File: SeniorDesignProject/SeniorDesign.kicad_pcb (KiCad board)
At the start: 2 copper layers, 33 parts, among them J1 RJ45(LoadCells), J2 RJ45(Accelerometer), J3 PICkit3, J5 ID-12LA Header, J6 XBEE Header, J7 7-Segment Display, P7 Power 1, P9 Power 2, U1 INA827, U2 LM1117-3.3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

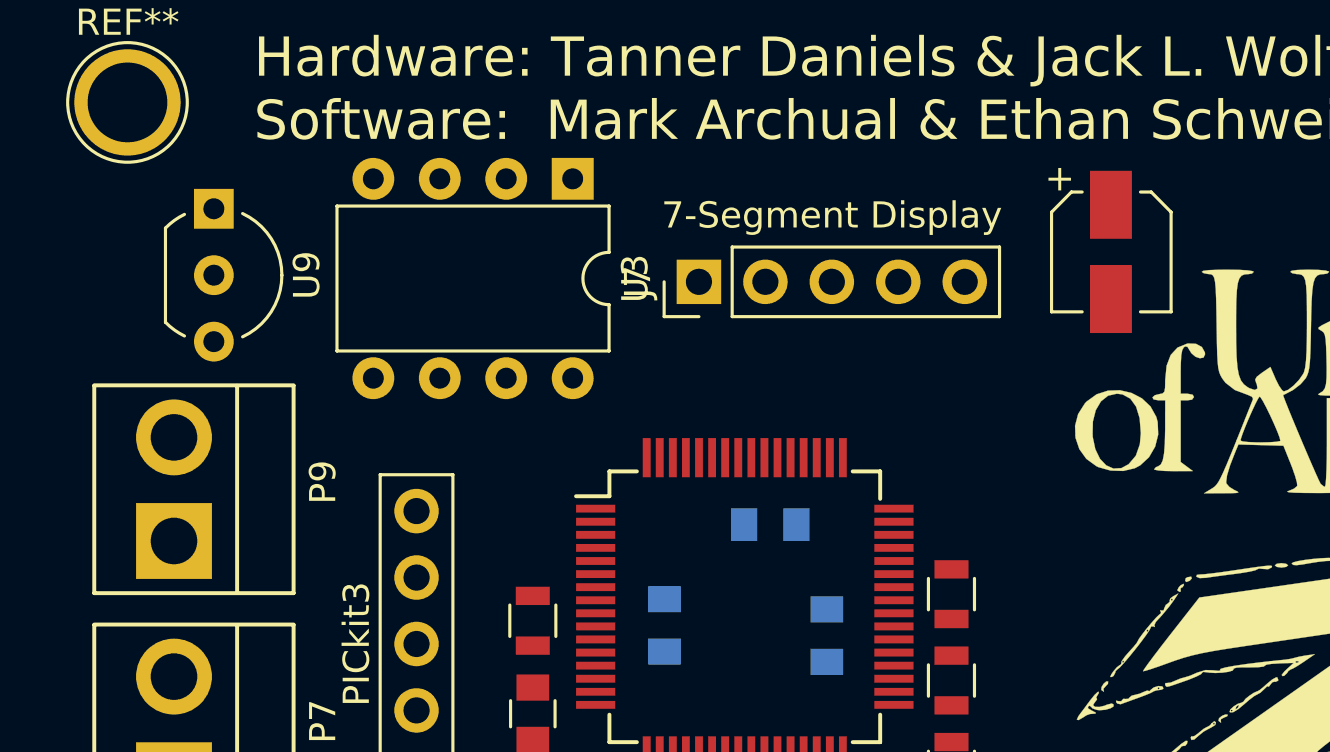
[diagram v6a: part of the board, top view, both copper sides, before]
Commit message: Added TC7660 +5V to -5V converter Removed -9V power Removed 7905 -9V to -5V regulator
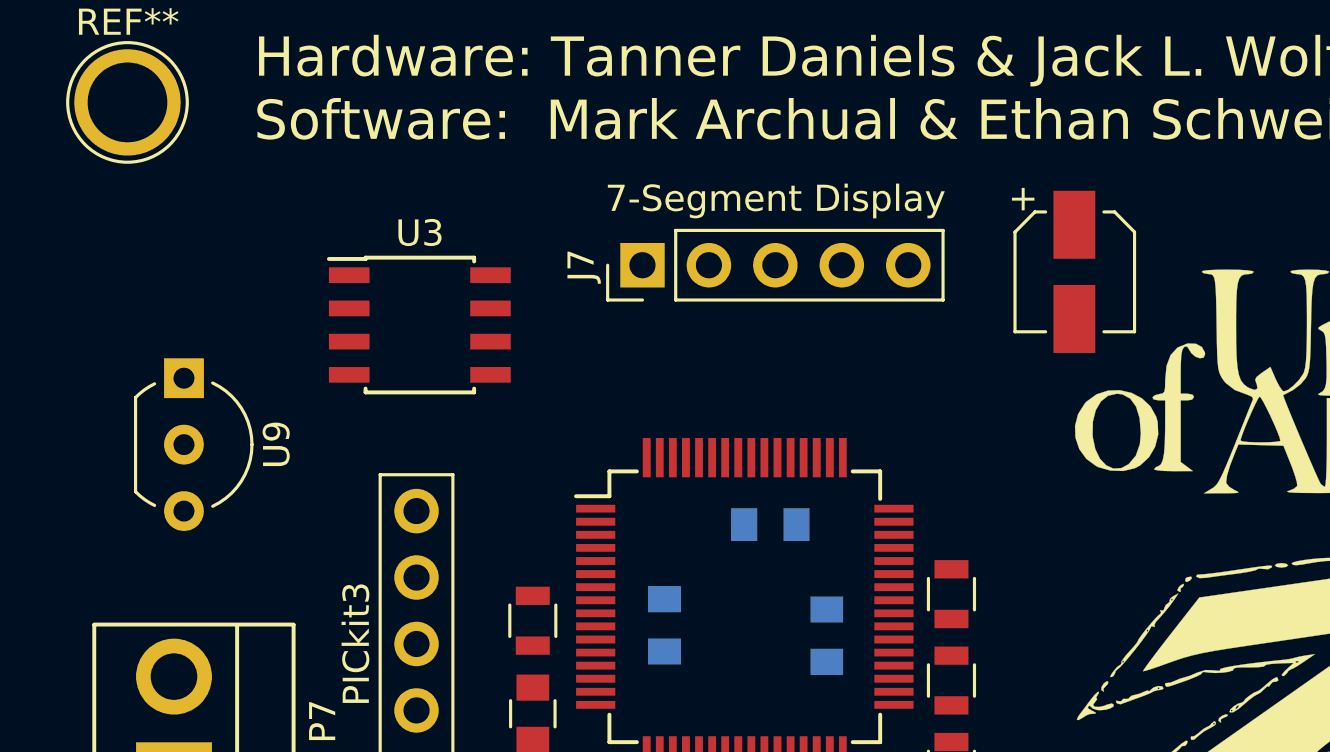
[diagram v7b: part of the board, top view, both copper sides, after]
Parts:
- removed P9: Power 2, Pin_Headers:Pin_Header_Straight_1x02_Pitch3.96mm_Friction_Lock
- U3: footprint Housings_DIP:DIP-8_W7.62mm -> Housings_SOIC:SOIC-8_3.9x4.9mm_Pitch1.27mm
- moved U3 8.08 mm to (131.3, 68.7), turned to 0 degrees
- moved U9 6.58 mm to (122.3, 70.7)
- moved J7 2.25 mm to (139.8, 66.4)
- moved C8 1.59 mm to (156.3, 66.7)
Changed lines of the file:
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@@
 (kicad_pcb (version 4) (host pcbnew 4.0.6-e0-6349~53~ubuntu16.04.1)
   (general
-    (links 66)
-    (no_connects 66)
-    (area 116.739999 56.175 186.028001 121.766001)
+    (links 65)
+    (no_connects 65)
+    (area 0 0 0 0)
     (thickness 1.6)
     (drawings 6)
     (tracks 2)
     (zones 0)
-    (modules 33)
-    (nets 103)
+    (modules 32)
+    (nets 102)
   )
   (page USLetter)
@@
   (net 95 "Net-(CPU1-Pad51)")
   (net 96 +9V)
-  (net 97 -9V)
-  (net 98 "Net-(U3-Pad1)")
-  (net 99 "Net-(U3-Pad2)")
-  (net 100 "Net-(U3-Pad6)")
-  (net 101 "Net-(U3-Pad7)")
-  (net 102 "Net-(U3-Pad4)")
+  (net 97 "Net-(U3-Pad1)")
+  (net 98 "Net-(U3-Pad2)")
+  (net 99 "Net-(U3-Pad6)")
+  (net 100 "Net-(U3-Pad7)")
+  (net 101 "Net-(U3-Pad4)")
   (net_class Default "This is the default net class."
     (clearance 0.2)
@@
     (add_net +9V)
     (add_net -5V)
-    (add_net -9V)
     (add_net 3.3V)
     (add_net A+)
@@
   )
   (module Capacitors_SMD:CP_Elec_4x4.5 (layer F.Cu)
-    (at 157.734 65.913 270)
+    (at 156.337 66.675 270)
     (descr "SMT capacitor, aluminium electrolytic, 4x4.5")
     (attr smd)
@@
     (pad 2 thru_hole circle (at 3.96 0 90) (size 2.9 2.9) (drill 1.78) (layers *.Cu *.Mask)
       (net 96 +9V))
-    (model Pin_Headers.3dshapes/Pin_Header_Straight_1x02_Pitch3.96mm_Friction_Lock.wrl
-      (at (xyz 0.08 0 0.125))
-      (scale (xyz 0.39 0.39 0.39))
-      (rotate (xyz 0 0 180))
-    )
-  )
-  (module Pin_Headers:Pin_Header_Straight_1x02_Pitch3.96mm_Friction_Lock (layer F.Cu)
-    (at 121.92 76.962 90)
-    (descr "Header Pin, Unshrouded, Friction Lock, Pitch 0.156\" (3.96mm)")
-    (tags "Pin Header Straight 1x02 Pitch3.96mm 640445-2")
-    (fp_text reference P9 (at 2.25 5.7 90) (layer F.SilkS)
-      (effects (font (size 1 1) (thickness 0.15)))
-    )
-    (fp_text value "Power 2" (at 2.45 -4.15 90) (layer F.Fab)
-      (effects (font (size 1 1) (thickness 0.15)))
-    )
-    (fp_line (start -2.25 -3.3) (end 6.2 -3.3) (layer F.CrtYd) (width 0.05))
-    (fp_line (start 6.2 -3.3) (end 6.2 4.85) (layer F.CrtYd) (width 0.05))
-    (fp_line (start 6.2 4.85) (end -2.25 4.85) (layer F.CrtYd) (width 0.05))
-    (fp_line (start -2.25 4.85) (end -2.25 -3.3) (layer F.CrtYd) (width 0.05))
-    (fp_line (start -1.9939 -3.048) (end 5.9309 -3.048) (layer F.SilkS) (width 0.15))
-    (fp_line (start -1.9939 4.572) (end 5.9309 4.572) (layer F.SilkS) (width 0.15))
-    (fp_line (start -1.9939 2.413) (end 5.9309 2.413) (layer F.SilkS) (width 0.15))
-    (fp_line (start 5.95 -3.048) (end 5.95 4.572) (layer F.SilkS) (width 0.15))
-    (fp_line (start -1.9939 -3.048) (end -1.9939 4.572) (layer F.SilkS) (width 0.15))
-    (pad 1 thru_hole rect (at 0 0 90) (size 2.9 2.9) (drill 1.78) (layers *.Cu *.Mask)
-      (net 97 -9V))
-    (pad 2 thru_hole circle (at 3.96 0 90) (size 2.9 2.9) (drill 1.78) (layers *.Cu *.Mask)
-      (net 45 GND))
     (model Pin_Headers.3dshapes/Pin_Header_Straight_1x02_Pitch3.96mm_Friction_Lock.wrl
       (at (xyz 0.08 0 0.125))
@@
   )
   (module Socket_Strips:Socket_Strip_Straight_1x05_Pitch2.54mm (layer F.Cu)
-    (at 141.986 67.056 90)
+    (at 139.827 66.421 90)
     (descr "Through hole straight socket strip, 1x05, 2.54mm pitch, single row")
     (tags "Through hole socket strip THT 1x05 2.54mm single row")
@@
   )
   (module TO_SOT_Packages_THT:TO-92_Inline_Wide (layer F.Cu)
-    (at 123.444 64.262 270)
+    (at 122.301 70.739 270)
     (descr "TO-92 leads in-line, wide, drill 0.8mm (see NXP sot054_po.pdf)")
     (tags "to-92 sc-43 sc-43a sot54 PA33 transistor")
@@
     (pad 1 thru_hole circle (at 0 0) (size 4.064 4.064) (drill 3.048) (layers *.Cu *.Mask))
   )
-  (module Housings_DIP:DIP-8_W7.62mm (layer F.Cu)
-    (at 137.16 63.119 270)
-    (descr "8-lead dip package, row spacing 7.62 mm (300 mils)")
-    (tags "DIL DIP PDIP 2.54mm 7.62mm 300mil")
-    (fp_text reference U3 (at 3.81 -2.39 270) (layer F.SilkS)
-      (effects (font (size 1 1) (thickness 0.15)))
-    )
-    (fp_text value ICL7660 (at 3.81 10.01 270) (layer F.Fab)
-      (effects (font (size 1 1) (thickness 0.15)))
-    )
-    (fp_arc (start 3.81 -1.39) (end 2.81 -1.39) (angle -180) (layer F.SilkS) (width 0.12))
-    (fp_line (start 1.635 -1.27) (end 6.985 -1.27) (layer F.Fab) (width 0.1))
-    (fp_line (start 6.985 -1.27) (end 6.985 8.89) (layer F.Fab) (width 0.1))
-    (fp_line (start 6.985 8.89) (end 0.635 8.89) (layer F.Fab) (width 0.1))
-    (fp_line (start 0.635 8.89) (end 0.635 -0.27) (layer F.Fab) (width 0.1))
-    (fp_line (start 0.635 -0.27) (end 1.635 -1.27) (layer F.Fab) (width 0.1))
-    (fp_line (start 2.81 -1.39) (end 1.04 -1.39) (layer F.SilkS) (width 0.12))
-    (fp_line (start 1.04 -1.39) (end 1.04 9.01) (layer F.SilkS) (width 0.12))
-    (fp_line (start 1.04 9.01) (end 6.58 9.01) (layer F.SilkS) (width 0.12))
-    (fp_line (start 6.58 9.01) (end 6.58 -1.39) (layer F.SilkS) (width 0.12))
-    (fp_line (start 6.58 -1.39) (end 4.81 -1.39) (layer F.SilkS) (width 0.12))
-    (fp_line (start -1.1 -1.6) (end -1.1 9.2) (layer F.CrtYd) (width 0.05))
-    (fp_line (start -1.1 9.2) (end 8.7 9.2) (layer F.CrtYd) (width 0.05))
-    (fp_line (start 8.7 9.2) (end 8.7 -1.6) (layer F.CrtYd) (width 0.05))
-    (fp_line (start 8.7 -1.6) (end -1.1 -1.6) (layer F.CrtYd) (width 0.05))
-    (pad 1 thru_hole rect (at 0 0 270) (size 1.6 1.6) (drill 0.8) (layers *.Cu *.Mask)
-      (net 98 "Net-(U3-Pad1)"))
-    (pad 5 thru_hole oval (at 7.62 7.62 270) (size 1.6 1.6) (drill 0.8) (layers *.Cu *.Mask)
+  (module Housings_SOIC:SOIC-8_3.9x4.9mm_Pitch1.27mm (layer F.Cu)
+    (at 131.318 68.707)
+    (descr "8-Lead Plastic Small Outline (SN) - Narrow, 3.90 mm Body [SOIC] (see Microchip Packaging Specification 00000049BS.pdf)")
+    (tags "SOIC 1.27")
+    (attr smd)
+    (fp_text reference U3 (at 0 -3.5) (layer F.SilkS)
+      (effects (font (size 1 1) (thickness 0.15)))
+    )
+    (fp_text value ICL7660 (at 0 3.5) (layer F.Fab)
+      (effects (font (size 1 1) (thickness 0.15)))
+    )
+    (fp_line (start -0.95 -2.45) (end 1.95 -2.45) (layer F.Fab) (width 0.15))
+    (fp_line (start 1.95 -2.45) (end 1.95 2.45) (layer F.Fab) (width 0.15))
+    (fp_line (start 1.95 2.45) (end -1.95 2.45) (layer F.Fab) (width 0.15))
+    (fp_line (start -1.95 2.45) (end -1.95 -1.45) (layer F.Fab) (width 0.15))
+    (fp_line (start -1.95 -1.45) (end -0.95 -2.45) (layer F.Fab) (width 0.15))
+    (fp_line (start -3.75 -2.75) (end -3.75 2.75) (layer F.CrtYd) (width 0.05))
+    (fp_line (start 3.75 -2.75) (end 3.75 2.75) (layer F.CrtYd) (width 0.05))
+    (fp_line (start -3.75 -2.75) (end 3.75 -2.75) (layer F.CrtYd) (width 0.05))
+    (fp_line (start -3.75 2.75) (end 3.75 2.75) (layer F.CrtYd) (width 0.05))
+    (fp_line (start -2.075 -2.575) (end -2.075 -2.525) (layer F.SilkS) (width 0.15))
+    (fp_line (start 2.075 -2.575) (end 2.075 -2.43) (layer F.SilkS) (width 0.15))
+    (fp_line (start 2.075 2.575) (end 2.075 2.43) (layer F.SilkS) (width 0.15))
+    (fp_line (start -2.075 2.575) (end -2.075 2.43) (layer F.SilkS) (width 0.15))
+    (fp_line (start -2.075 -2.575) (end 2.075 -2.575) (layer F.SilkS) (width 0.15))
+    (fp_line (start -2.075 2.575) (end 2.075 2.575) (layer F.SilkS) (width 0.15))
+    (fp_line (start -2.075 -2.525) (end -3.475 -2.525) (layer F.SilkS) (width 0.15))
+    (pad 1 smd rect (at -2.7 -1.905) (size 1.55 0.6) (layers F.Cu F.Paste F.Mask)
+      (net 97 "Net-(U3-Pad1)"))
+    (pad 2 smd rect (at -2.7 -0.635) (size 1.55 0.6) (layers F.Cu F.Paste F.Mask)
+      (net 98 "Net-(U3-Pad2)"))
+    (pad 3 smd rect (at -2.7 0.635) (size 1.55 0.6) (layers F.Cu F.Paste F.Mask)
+      (net 45 GND))
+    (pad 4 smd rect (at -2.7 1.905) (size 1.55 0.6) (layers F.Cu F.Paste F.Mask)
+      (net 101 "Net-(U3-Pad4)"))
+    (pad 5 smd rect (at 2.7 1.905) (size 1.55 0.6) (layers F.Cu F.Paste F.Mask)
       (net 46 -5V))
-    (pad 2 thru_hole oval (at 0 2.54 270) (size 1.6 1.6) (drill 0.8) (layers *.Cu *.Mask)
-      (net 99 "Net-(U3-Pad2)"))
-    (pad 6 thru_hole oval (at 7.62 5.08 270) (size 1.6 1.6) (drill 0.8) (layers *.Cu *.Mask)
-      (net 100 "Net-(U3-Pad6)"))
-    (pad 3 thru_hole oval (at 0 5.08 270) (size 1.6 1.6) (drill 0.8) (layers *.Cu *.Mask)
-      (net 45 GND))
-    (pad 7 thru_hole oval (at 7.62 2.54 270) (size 1.6 1.6) (drill 0.8) (layers *.Cu *.Mask)
-      (net 101 "Net-(U3-Pad7)"))
-    (pad 4 thru_hole oval (at 0 7.62 270) (size 1.6 1.6) (drill 0.8) (layers *.Cu *.Mask)
-      (net 102 "Net-(U3-Pad4)"))
-    (pad 8 thru_hole oval (at 7.62 0 270) (size 1.6 1.6) (drill 0.8) (layers *.Cu *.Mask)
+    (pad 6 smd rect (at 2.7 0.635) (size 1.55 0.6) (layers F.Cu F.Paste F.Mask)
+      (net 99 "Net-(U3-Pad6)"))
+    (pad 7 smd rect (at 2.7 -0.635) (size 1.55 0.6) (layers F.Cu F.Paste F.Mask)
+      (net 100 "Net-(U3-Pad7)"))
+    (pad 8 smd rect (at 2.7 -1.905) (size 1.55 0.6) (layers F.Cu F.Paste F.Mask)
       (net 51 +5V))
-    (model Housings_DIP.3dshapes/DIP-8_W7.62mm.wrl
+    (model Housings_SOIC.3dshapes/SOIC-8_3.9x4.9mm_Pitch1.27mm.wrl
       (at (xyz 0 0 0))
       (scale (xyz 1 1 1))

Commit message: Made more changes to board design and layout
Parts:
- moved R1 44.6 mm to (165.4, 97.3)
- moved J3 41.6 mm to (171.7, 98.0)
- moved U1 35.1 mm to (144.3, 70.4), turned to 180 degrees
- moved U2 30.0 mm to (130.8, 78.2), turned to 270 degrees
- moved C2 26.6 mm to (136.7, 70.1), turned to 180 degrees
- moved C1 19.6 mm to (125.2, 72.1)
- moved J1 13.5 mm to (145.3, 106.7)
- moved J6 11.6 mm to (127.5, 101.9)
- moved J2 11.1 mm to (165.9, 106.7)
- moved C4 7.01 mm to (140.7, 88.4), turned to 90 degrees
- moved P7 5.64 mm to (121.2, 80.5)
- moved U9 4.74 mm to (120.7, 66.3)
- moved U3 3.19 mm to (130.0, 65.8)
- moved R4 1.61 mm to (147.1, 88.1), turned to 90 degrees
- moved C3 0.57 mm to (144.0, 88.1), turned to 270 degrees
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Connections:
- C2 pad 2: Net-(C2-Pad2) -> GND
- U9 pad 1: (no net) -> +5V
- U9 pad 2: (no net) -> GND
- U9 pad 3: (no net) -> +9V
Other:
- board outline added: 69.1 x 65.3 mm
